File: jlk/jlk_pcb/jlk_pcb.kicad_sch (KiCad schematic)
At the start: 44 parts, among them SW12 SWITCH_PUSH, SW13 SWITCH_PUSH, SW14 SWITCH_PUSH, SW17 SWITCH_PUSH, SW18 SWITCH_PUSH, SW19 SWITCH_PUSH, SW20 SWITCH_PUSH, SW22 SWITCH_PUSH, SW23 SWITCH_PUSH, SW24 SWITCH_PUSH, SW25 SWITCH_PUSH, SW27 SWITCH_PUSH, SW28 SWITCH_PUSH, SW29 SWITCH_PUSH, SW30 SWITCH_PUSH, SW34 SWITCH_PUSH, SW35 SWITCH_PUSH, SW36 SWITCH_PUSH, SW37 SWITCH_PUSH, SW39 SWITCH_PUSH, SW40 SWITCH_PUSH, SW41 SWITCH_PUSH, SW42 SWITCH_PUSH, SW44 SWITCH_PUSH, SW45 SWITCH_PUSH, SW46 SWITCH_PUSH, SW47 SWITCH_PUSH, SW49 SWITCH_PUSH, SW50 SWITCH_PUSH, SW51 SWITCH_PUSH, SW54 SWITCH_PUSH, SW55 SWITCH_PUSH, SW56 SWITCH_PUSH, SW7 SWITCH_PUSH, SW8 SWITCH_PUSH, SW9 SWITCH_PUSH, U1 ARDUINO_PRO_MICRO

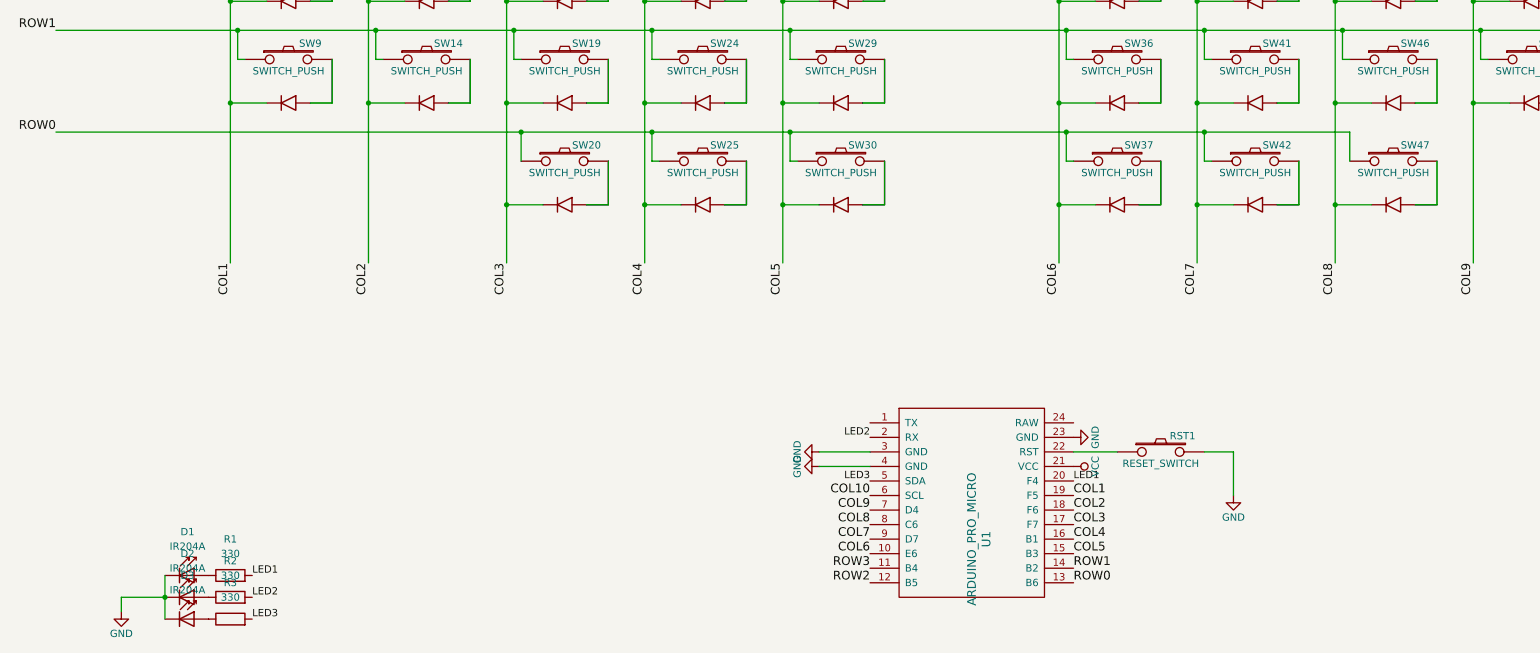
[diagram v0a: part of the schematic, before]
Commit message: Renamed jl142 to jlk.
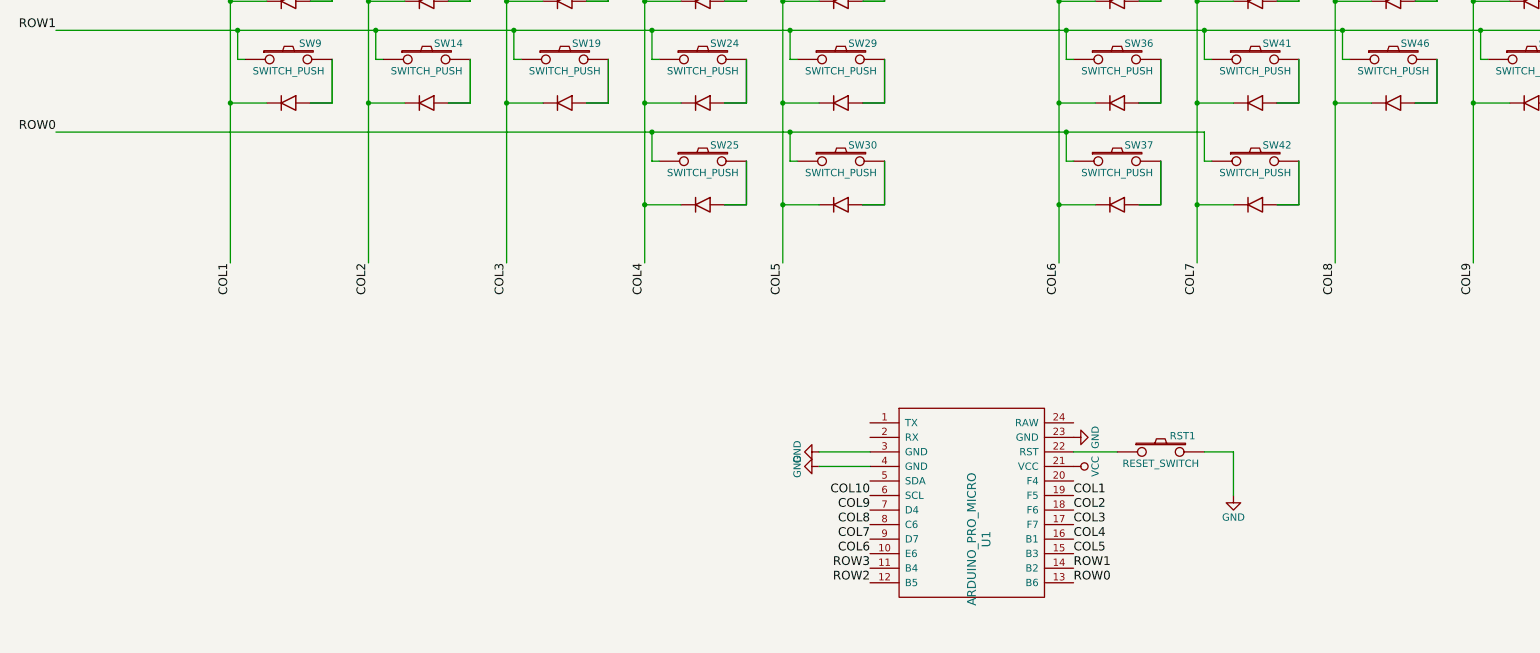
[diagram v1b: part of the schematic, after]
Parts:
- removed D1, D2, D3: IR204A, LED_THT:LED_D3.0mm_IRBlack, symbol LED:IR204A
- removed R1, R2, R3: 330, Resistor_THT:R_Axial_DIN0207_L6.3mm_D2.5mm_P7.62mm_Horizontal, symbol Device:R
- removed SW20, SW47: SWITCH_PUSH, footprints:cherry_hotswap_with_diode, symbol symbols:SWITCH_WITH_DIODE
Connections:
- net LED1: no longer names the net of U1.20 (F4)
- net LED2: no longer names the net of U1.2 (RX)
- net LED3: no longer names the net of U1.5 (SDA)

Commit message: Final? design of jlk before fillet and creating plates.
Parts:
- added H0, H1, H10, H11, H2, H3, H4, H5, H6, H7, H8, H9: MountingHole_Pad, MountingHole:MountingHole_2.2mm_M2_ISO7380_Pad, symbol Mechanical:MountingHole_Pad
- added H12, H13, H14, H15: MountingHole, MountingHole:MountingHole_3.5mm, symbol Mechanical:MountingHole
- RST0: renamed from RST1; footprint footprints:reset_button -> footprints:kailh_choc
- renumbered SW7 to SW0, SW8 to SW1, SW23 to SW10, SW24 to SW11, SW25 to SW12, SW27 to SW13, SW28 to SW14, SW29 to SW15, SW30 to SW16, SW34 to SW17, SW35 to SW18, SW36 to SW19, SW9 to SW2, SW37 to SW20, SW39 to SW21, SW40 to SW22, SW41 to SW23, SW42 to SW24, SW44 to SW25, SW45 to SW26, SW46 to SW27, SW49 to SW28, SW50 to SW29, SW12 to SW3, SW51 to SW30, SW54 to SW31, SW55 to SW32, SW56 to SW33, SW13 to SW4, SW14 to SW5, SW17 to SW6, SW18 to SW7, SW19 to SW8, SW22 to SW9, U1 to U0
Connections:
- net COL1: now also U0.20 (F4); no longer U0.19 (F5)
- net COL10: now also U0.5 (SDA); no longer U0.6 (SCL)
- net COL2: now also U0.19 (F5); no longer U0.18 (F6)
- net COL3: now also U0.18 (F6); no longer U0.17 (F7)
- net COL4: now also U0.17 (F7); no longer U0.16 (B1)
- net COL5: now also U0.16 (B1); no longer U0.15 (B3)
- net COL6: now also U0.9 (D7); no longer U0.10 (E6)
- net COL7: now also U0.8 (C6); no longer U0.9 (D7)
- net COL8: now also U0.7 (D4); no longer U0.8 (C6)
- net COL9: now also U0.6 (SCL); no longer U0.7 (D4)
- net GND: now also H0.1, H1.1, H10.1, H11.1, H2.1, H3.1, H4.1, H5.1, H6.1, H7.1, H8.1, H9.1

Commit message: Switched to SMD diode, col2row.
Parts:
- removed H12, H13, H14, H15: MountingHole, MountingHole:MountingHole_3.5mm, symbol Mechanical:MountingHole
- H0, H1, H10, H11, H2, H3, H4, H5, H6, H7, H8, H9: value MountingHole_Pad -> MountingHole; footprint MountingHole:MountingHole_2.2mm_M2_ISO7380_Pad -> MountingHole:MountingHole_3.5mm; symbol Mechanical:MountingHole_Pad -> Mechanical:MountingHole
- U0: footprint footprints:ARDUINO_PRO_MICRO -> ProMicro_v2
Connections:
- net COL1: now also SW0.1, SW1.1, SW2.1; no longer SW0.3 (K), SW1.3 (K), SW2.3 (K)
- net COL10: now also SW31.1, SW32.1, SW33.1; no longer SW31.3 (K), SW32.3 (K), SW33.3 (K)
- net COL2: now also SW3.1, SW4.1, SW5.1; no longer SW3.3 (K), SW4.3 (K), SW5.3 (K)
- net COL3: now also SW6.1, SW7.1, SW8.1; no longer SW6.3 (K), SW7.3 (K), SW8.3 (K)
- net COL4: now also SW10.1, SW11.1, SW12.1, SW9.1; no longer SW10.3 (K), SW11.3 (K), SW12.3 (K), SW9.3 (K)
- net COL5: now also SW13.1, SW14.1, SW15.1, SW16.1; no longer SW13.3 (K), SW14.3 (K), SW15.3 (K), SW16.3 (K)
- net COL6: now also SW17.1, SW18.1, SW19.1, SW20.1; no longer SW17.3 (K), SW18.3 (K), SW19.3 (K), SW20.3 (K)
- net COL7: now also SW21.1, SW22.1, SW23.1, SW24.1; no longer SW21.3 (K), SW22.3 (K), SW23.3 (K), SW24.3 (K)
- net COL8: now also SW25.1, SW26.1, SW27.1; no longer SW25.3 (K), SW26.3 (K), SW27.3 (K)
- net COL9: now also SW28.1, SW29.1, SW30.1; no longer SW28.3 (K), SW29.3 (K), SW30.3 (K)
- net GND: no longer H0.1, H1.1, H10.1, H11.1, H2.1, H3.1, H4.1, H5.1, H6.1, H7.1, H8.1, H9.1
- net ROW0: now also SW12.3 (K), SW16.3 (K), SW20.3 (K), SW24.3 (K); no longer SW12.1, SW16.1, SW20.1, SW24.1
- net ROW1: now also SW11.3 (K), SW15.3 (K), SW19.3 (K), SW2.3 (K), SW23.3 (K), SW27.3 (K), SW30.3 (K), SW33.3 (K), SW5.3 (K), SW8.3 (K); no longer SW11.1, SW15.1, SW19.1, SW2.1, SW23.1, SW27.1, SW30.1, SW33.1, SW5.1, SW8.1
- net ROW2: now also SW1.3 (K), SW10.3 (K), SW14.3 (K), SW18.3 (K), SW22.3 (K), SW26.3 (K), SW29.3 (K), SW32.3 (K), SW4.3 (K), SW7.3 (K); no longer SW1.1, SW10.1, SW14.1, SW18.1, SW22.1, SW26.1, SW29.1, SW32.1, SW4.1, SW7.1
- net ROW3: now also SW0.3 (K), SW13.3 (K), SW17.3 (K), SW21.3 (K), SW25.3 (K), SW28.3 (K), SW3.3 (K), SW31.3 (K), SW6.3 (K), SW9.3 (K); no longer SW0.1, SW13.1, SW17.1, SW21.1, SW25.1, SW28.1, SW3.1, SW31.1, SW6.1, SW9.1

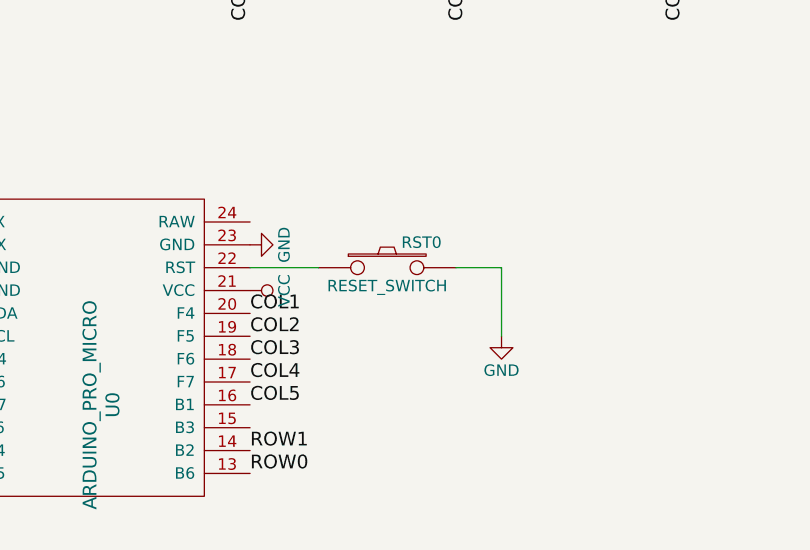
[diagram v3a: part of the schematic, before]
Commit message: Changed the reset button on the jlk.
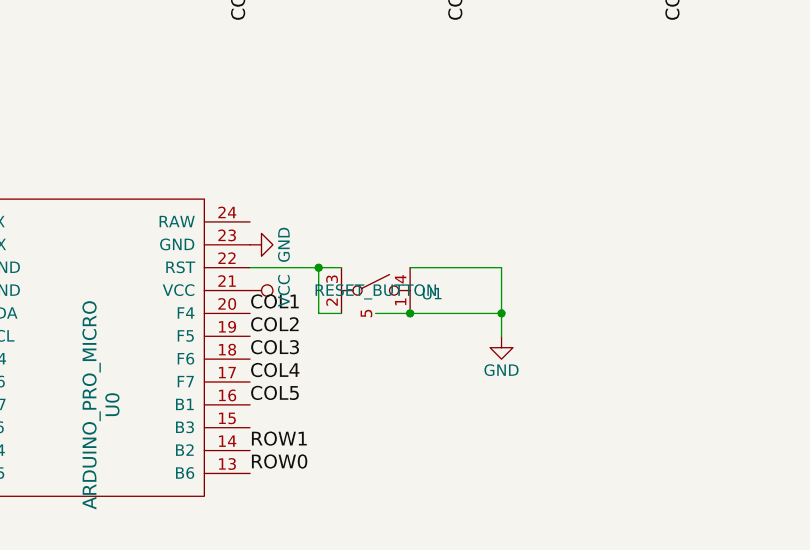
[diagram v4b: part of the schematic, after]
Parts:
- removed RST0: RESET_SWITCH, footprints:kailh_choc, symbol symbols:SWITCH_PUSH
- added U1: RESET_BUTTON, footprints:reset_button_1, symbol symbols:RESET_BUTTON
- U0: footprint ProMicro_v2 -> footprints:ARDUINO_PRO_MICRO
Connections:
- net GND: now also U1.1, U1.4, U1.5
- net at U0.22 (RST): now also U1.2, U1.3
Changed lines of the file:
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@@
 (kicad_sch (version 20230121) (generator eeschema)
   (paper "USLedger")
+  (junction (at 226.06 154.94) (diameter 0) (color 0 0 0 0)
+  )
   (junction (at 294.64 63.5) (diameter 0) (color 0 0 0 0)
   )
@@
   (junction (at 285.75 71.12) (diameter 0) (color 0 0 0 0)
   )
+  (junction (at 205.74 149.86) (diameter 0) (color 0 0 0 0)
+  )
   (junction (at 53.34 81.28) (diameter 0) (color 0 0 0 0)
   )
+  (junction (at 215.9 154.94) (diameter 0) (color 0 0 0 0)
+  )
   (junction (at 149.86 63.5) (diameter 0) (color 0 0 0 0)
   )
@@
     (stroke (width 0) (type default))
   )
+  (wire (pts (xy 215.9 154.94) (xy 226.06 154.94))
+    (stroke (width 0) (type default))
+  )
   (wire (pts (xy 92.71 88.9) (xy 116.84 88.9))
     (stroke (width 0) (type default))
@@
     (stroke (width 0) (type default))
   )
-  (wire (pts (xy 226.06 149.86) (xy 226.06 157.48))
+  (wire (pts (xy 226.06 149.86) (xy 226.06 154.94))
     (stroke (width 0) (type default))
   )
@@
     (stroke (width 0) (type default))
   )
-  (wire (pts (xy 220.98 149.86) (xy 226.06 149.86))
+  (wire (pts (xy 215.9 149.86) (xy 226.06 149.86))
     (stroke (width 0) (type default))
   )
@@
     (stroke (width 0) (type default))
   )
+  (wire (pts (xy 212.09 154.94) (xy 215.9 154.94))
+    (stroke (width 0) (type default))
+  )
   (wire (pts (xy 92.71 71.12) (xy 116.84 71.12))
     (stroke (width 0) (type default))
   )
+  (wire (pts (xy 208.28 154.94) (xy 205.74 154.94))
+    (stroke (width 0) (type default))
+  )
   (wire (pts (xy 77.47 81.28) (xy 77.47 116.84))
     (stroke (width 0) (type default))
@@
     (stroke (width 0) (type default))
   )
+  (wire (pts (xy 205.74 149.86) (xy 208.28 149.86))
+    (stroke (width 0) (type default))
+  )
   (wire (pts (xy 101.6 63.5) (xy 101.6 81.28))
     (stroke (width 0) (type default))
   )
+  (wire (pts (xy 205.74 154.94) (xy 205.74 149.86))
+    (stroke (width 0) (type default))
+  )
   (wire (pts (xy 270.51 81.28) (xy 270.51 116.84))
     (stroke (width 0) (type default))
@@
   )
   (wire (pts (xy 125.73 45.72) (xy 125.73 63.5))
+    (stroke (width 0) (type default))
+  )
+  (wire (pts (xy 226.06 154.94) (xy 226.06 157.48))
     (stroke (width 0) (type default))
   )
@@
       (effects (font (size 1.524 1.524)))
     )
-    (property "Footprint" "ProMicro_v2" (at 182.88 190.5 0)
+    (property "Footprint" "footprints:ARDUINO_PRO_MICRO" (at 182.88 190.5 0)
       (effects (font (size 1.524 1.524)) hide)
     )
@@
     )
   )
-  (symbol (lib_id "symbols:SWITCH_PUSH") (at 213.36 149.86 0) (unit 1)
-    (in_bom yes) (on_board yes) (dnp no)
-    (property "Reference" "RST0" (at 217.17 147.066 0)
-      (effects (font (size 1.27 1.27)))
-    )
-    (property "Value" "RESET_SWITCH" (at 213.36 151.892 0)
-      (effects (font (size 1.27 1.27)))
-    )
-    (property "Footprint" "footprints:kailh_choc" (at 213.36 149.86 0)
-      (effects (font (size 1.524 1.524)) hide)
-    )
-    (property "Datasheet" "" (at 213.36 149.86 0)
-      (effects (font (size 1.524 1.524)) hide)
-    )
-    (pin "1")
-    (pin "2")
-    (instances
-      (project "jlk_pcb"
-        (path "/97127b28-60f4-45ff-835e-dccfbc833331"
-          (reference "RST0") (unit 1)
-        )
-      )
-    )
-  )
   (symbol (lib_id "Atreus62-rescue:GND") (at 226.06 157.48 0) (unit 1)
     (in_bom yes) (on_board yes) (dnp no)
@@
         )
       )
+    )
+  )
+  (symbol (lib_id "symbols:RESET_BUTTON") (at 212.09 152.4 270) (unit 1)
+    (in_bom yes) (on_board yes) (dnp no) (fields_autoplaced)
+    (property "Reference" "U1" (at 217.17 152.781 90)
+      (effects (font (size 1.27 1.27)) (justify left))
+    )
+    (property "Value" "RESET_BUTTON" (at 212.09 152.4 90)
+      (effects (font (size 1.27 1.27)))
+    )
+    (property "Footprint" "footprints:reset_button_1" (at 212.09 152.4 90)
+      (effects (font (size 1.27 1.27)) hide)
+    )
+    (property "Datasheet" "" (at 212.09 152.4 90)
+      (effects (font (size 1.27 1.27)) hide)
+    )
+    (pin "2")
+    (pin "3")
+    (pin "4")
+    (pin "5")
+    (pin "1")
+    (instances
+      (project "jlk_pcb"
+        (path "/97127b28-60f4-45ff-835e-dccfbc833331"
+          (reference "U1") (unit 1)
+        )
+      )
